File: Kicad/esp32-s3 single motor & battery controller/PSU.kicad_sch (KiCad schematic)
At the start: 74 parts, among them J5 Batt Balance connector, Q1 NMOS,12v, Q2 NMOS, 12v, Q3 NMOS,12v,PPak, Q4 NMOS, 12v, Q5 NMOS, 12v, Q7 NMOS,12v,PPak, U2 AP63203WU, U3 BQ76905RGRR, U4 BQ24780SRUYR

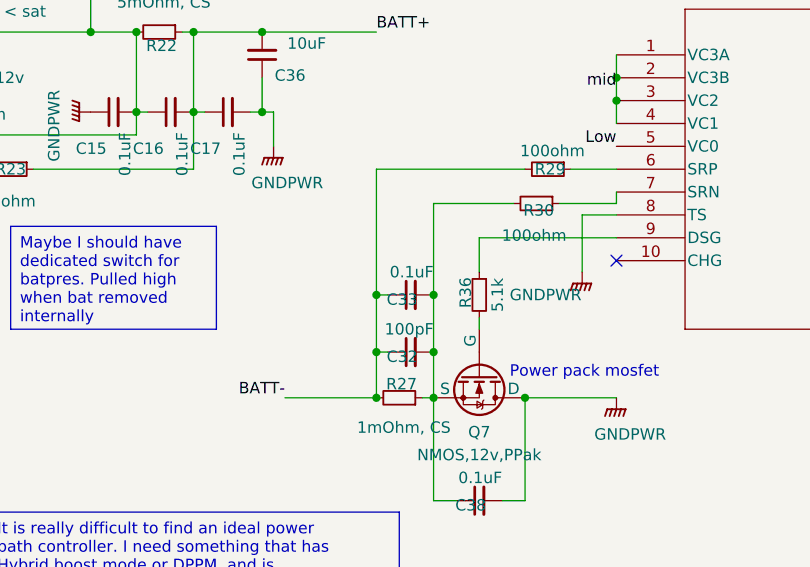
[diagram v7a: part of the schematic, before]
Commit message: Swapped sides for battery balance IC
This actually simplifies routing a lot, since the current sense lines are on the same side.
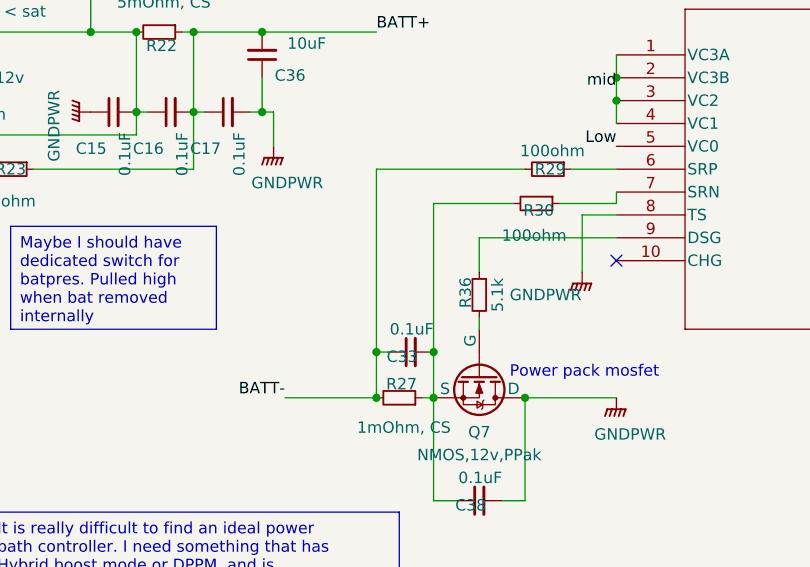
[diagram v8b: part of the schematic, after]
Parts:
- removed C32: 100pF, Capacitor_SMD:C_0603_1608Metric, symbol Device:C_Small
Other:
- moved on the sheet: C33
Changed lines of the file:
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@@
 	)
 	(junction
-		(at 157.48 147.32)
-		(diameter 0)
-		(color 0 0 0 0)
-	)
-	(junction
 		(at 137.16 127)
 		(diameter 0)
@@
 	)
 	(junction
-		(at 163.83 147.32)
-		(diameter 0)
-		(color 0 0 0 0)
-	)
-	(junction
 		(at 189.23 88.9)
 		(diameter 0)
@@
 	)
 	(junction
+		(at 163.83 153.67)
+		(diameter 0)
+		(color 0 0 0 0)
+	)
+	(junction
 		(at 234.95 130.81)
 		(diameter 0)
@@
 	)
 	(junction
-		(at 163.83 153.67)
-		(diameter 0)
-		(color 0 0 0 0)
-	)
-	(junction
 		(at 125.73 100.33)
 		(diameter 0)
@@
 	(wire
 		(pts
+			(xy 163.83 153.67) (xy 163.83 158.75)
+		)
+		(stroke
+			(width 0)
+			(type default)
+		)
+	)
+	(wire
+		(pts
 			(xy 163.83 170.18) (xy 163.83 158.75)
 		)
@@
 	(wire
 		(pts
-			(xy 163.83 137.16) (xy 163.83 147.32)
+			(xy 163.83 137.16) (xy 163.83 153.67)
 		)
 		(stroke
@@
 	(wire
 		(pts
-			(xy 158.75 147.32) (xy 157.48 147.32)
+			(xy 158.75 153.67) (xy 157.48 153.67)
 		)
 		(stroke
@@
 	(wire
 		(pts
-			(xy 163.83 153.67) (xy 163.83 147.32)
-		)
-		(stroke
-			(width 0)
-			(type default)
-		)
-	)
-	(wire
-		(pts
 			(xy 125.73 64.77) (xy 119.38 64.77)
 		)
@@
 	(wire
 		(pts
-			(xy 157.48 153.67) (xy 158.75 153.67)
-		)
-		(stroke
-			(width 0)
-			(type default)
-		)
-	)
-	(wire
-		(pts
 			(xy 93.98 166.37) (xy 93.98 161.29)
 		)
@@
 	(wire
 		(pts
-			(xy 163.83 158.75) (xy 163.83 153.67)
-		)
-		(stroke
-			(width 0)
-			(type default)
-		)
-	)
-	(wire
-		(pts
 			(xy 114.3 118.11) (xy 125.73 118.11)
 		)
@@
 	(wire
 		(pts
-			(xy 157.48 153.67) (xy 157.48 147.32)
+			(xy 157.48 133.35) (xy 157.48 153.67)
 		)
 		(stroke
@@
 	(wire
 		(pts
-			(xy 157.48 133.35) (xy 157.48 147.32)
-		)
-		(stroke
-			(width 0)
-			(type default)
-		)
-	)
-	(wire
-		(pts
 			(xy 97.79 118.11) (xy 101.6 118.11)
 		)
@@
 	)
 	(symbol
-		(lib_id "Device:C_Small")
-		(at 161.29 153.67 90)
-		(mirror x)
-		(unit 1)
-		(exclude_from_sim no)
-		(in_bom yes)
-		(on_board yes)
-		(dnp no)
-		(property "Reference" "C32"
-			(at 162.052 154.178 90)
-			(effects
-				(font
-					(size 1.27 1.27)
-				)
-				(justify left)
-			)
-		)
-		(property "Value" "100pF"
-			(at 163.83 151.13 90)
-			(effects
-				(font
-					(size 1.27 1.27)
-				)
-				(justify left)
-			)
-		)
-		(property "Footprint" "Capacitor_SMD:C_0603_1608Metric"
-			(at 161.29 153.67 0)
-			(effects
-				(font
-					(size 1.27 1.27)
-				)
-				(hide yes)
-			)
-		)
-		(property "Datasheet" "~"
-			(at 161.29 153.67 0)
-			(effects
-				(font
-					(size 1.27 1.27)
-				)
-				(hide yes)
-			)
-		)
-		(property "Description" "Unpolarized capacitor, small symbol"
-			(at 161.29 153.67 0)
-			(effects
-				(font
-					(size 1.27 1.27)
-				)
-				(hide yes)
-			)
-		)
-		(pin "1"
-		)
-		(pin "2"
-		)
-		(instances
-			(project "esp32-s3 single motor & battery controller"
-				(path "/eb3f183d-8bb1-43a5-a363-092ed67891e3/a57a0b4f-e246-497c-8d94-688647d8fd03"
-					(reference "C32")
-					(unit 1)
-				)
-			)
-		)
-	)
-	(symbol
 		(lib_id "Device:L")
 		(at 283.21 62.23 90)
@@
 	(symbol
 		(lib_id "Device:C_Small")
-		(at 161.29 147.32 90)
+		(at 161.29 153.67 90)
 		(mirror x)
 		(unit 1)
@@
 		(dnp no)
 		(property "Reference" "C33"
-			(at 162.052 147.828 90)
+			(at 162.052 154.178 90)
 			(effects
 				(font
@@
 		)
 		(property "Value" "0.1uF"
-			(at 163.83 144.78 90)
+			(at 163.83 151.13 90)
 			(effects
 				(font
@@
 		)
 		(property "Footprint" "Capacitor_SMD:C_0603_1608Metric"
-			(at 161.29 147.32 0)
+			(at 161.29 153.67 0)
 			(effects
 				(font
@@
 		)
 		(property "Datasheet" "~"
-			(at 161.29 147.32 0)
+			(at 161.29 153.67 0)
 			(effects
 				(font
@@
 		)
 		(property "Description" "Unpolarized capacitor, small symbol"
-			(at 161.29 147.32 0)
+			(at 161.29 153.67 0)
 			(effects
 				(font
